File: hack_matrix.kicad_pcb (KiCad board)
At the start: 11 copper layers, 30.9 x 26.7 mm, 16 parts, among them J1 USB_C_Receptacle_USB2.0_16P, J2 Screw_Terminal_01x02, SW2 SW_Push, U1 SN74AHCT245PWR, U3 XC6206P332MR, U4 ESP32-S2-MINI-2, U5 SN74AHCT245PWR

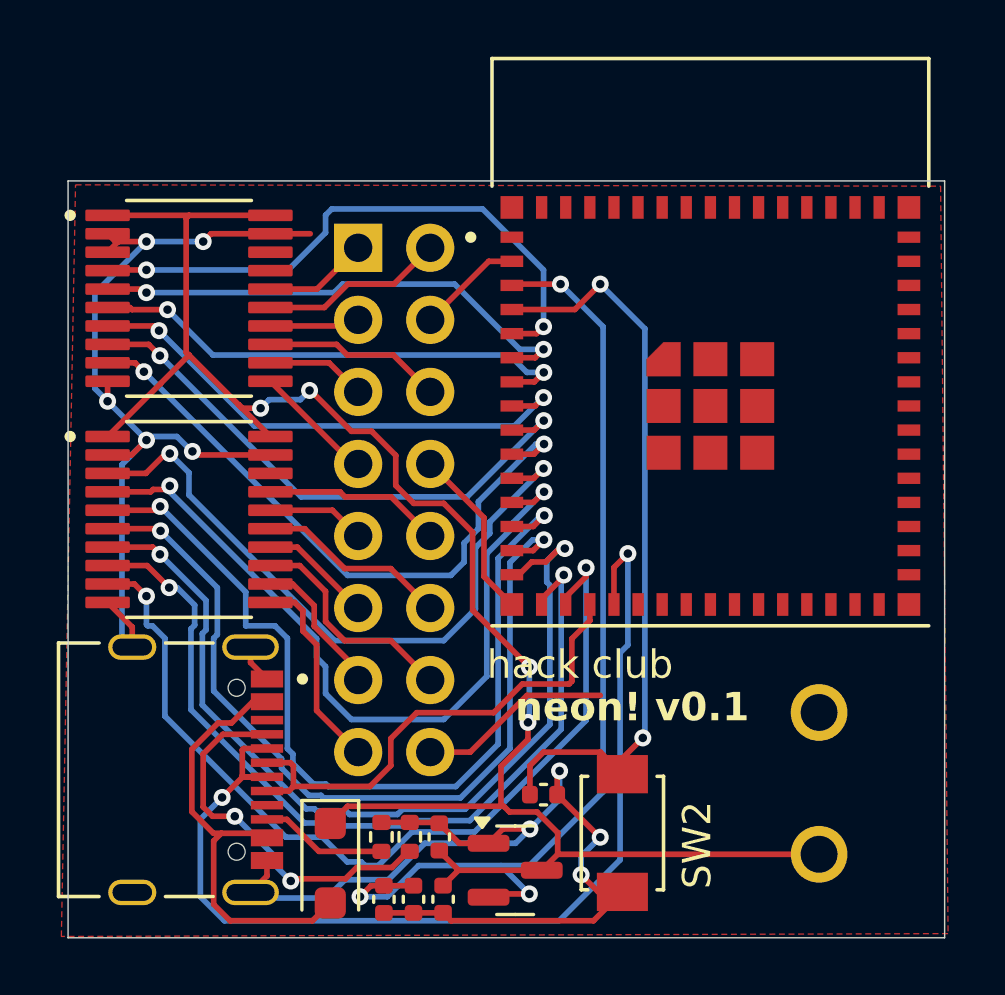
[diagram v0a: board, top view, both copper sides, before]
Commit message: update to fix USB wiring / EN pin.
TODO: fix screw jack part #
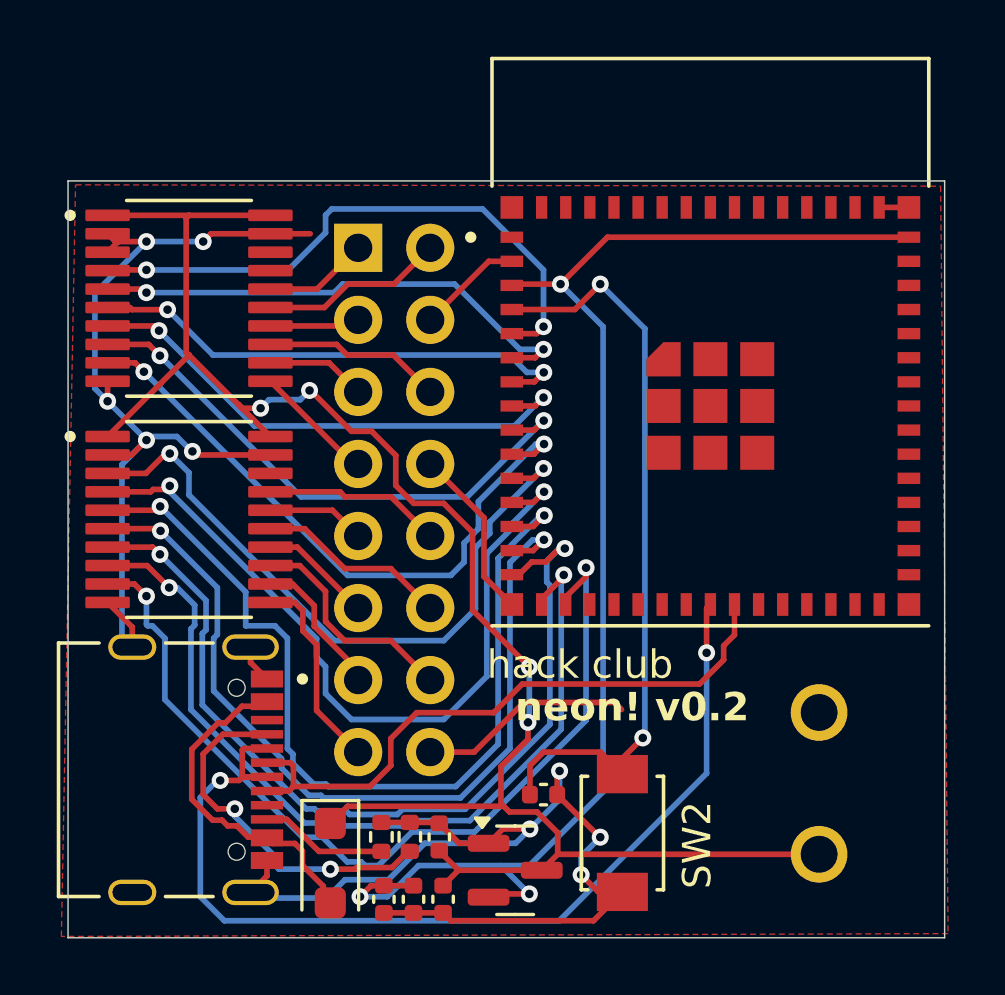
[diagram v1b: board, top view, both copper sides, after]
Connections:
- U4 pad 18: /D+ -> unconnected-(U4-IO14-Pad18)
- U4 pad 19: /D- -> unconnected-(U4-IO15-Pad19)
- U4 pad 23: unconnected-(U4-IO19-Pad23) -> /D-
- U4 pad 24: unconnected-(U4-IO20-Pad24) -> /D+
- U4 pad 45: unconnected-(U4-EN-Pad45) -> +3V3
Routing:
- net +3V3: track 35.3 -> 48.2 mm
- net /D+: track 17.6 -> 22.4 mm
- net Net-(D1-A): track 15.8 -> 12.0 mm
- net /D-: track 37.3 -> 35.2 mm
- net GND: track 87.0 -> 88.8 mm
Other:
- board text added: "neon! v0.2"
- board text removed: "neon! v0.1"
